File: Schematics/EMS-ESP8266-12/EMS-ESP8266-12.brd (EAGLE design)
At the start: 86 x 50.8 mm, 45 parts, among them IC1 LM393N, J99 Upload, T1 BC547B, T2 BC547B

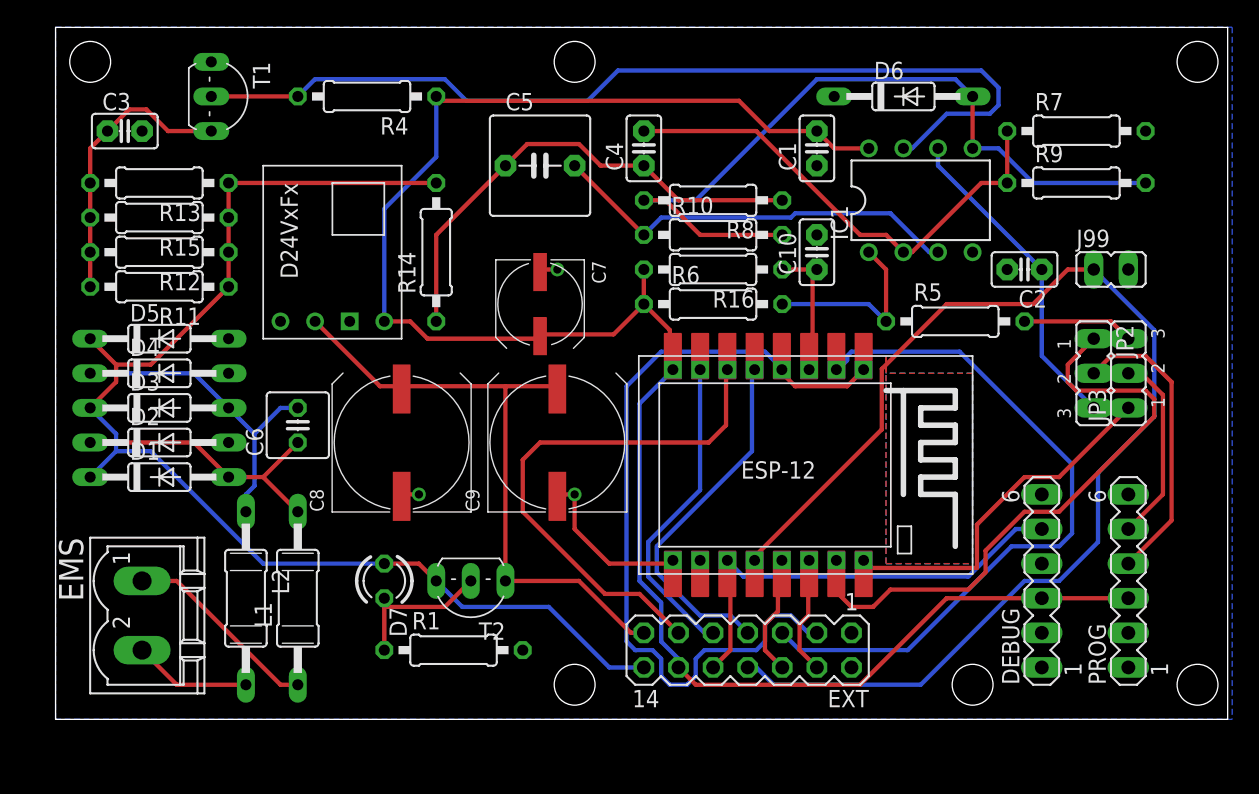
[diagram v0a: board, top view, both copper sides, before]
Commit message: PCB reworked ° remove ground layer below ESP12-antenna ° change connector footprint ° 2pin debug connector ° small form factor for EMS connector
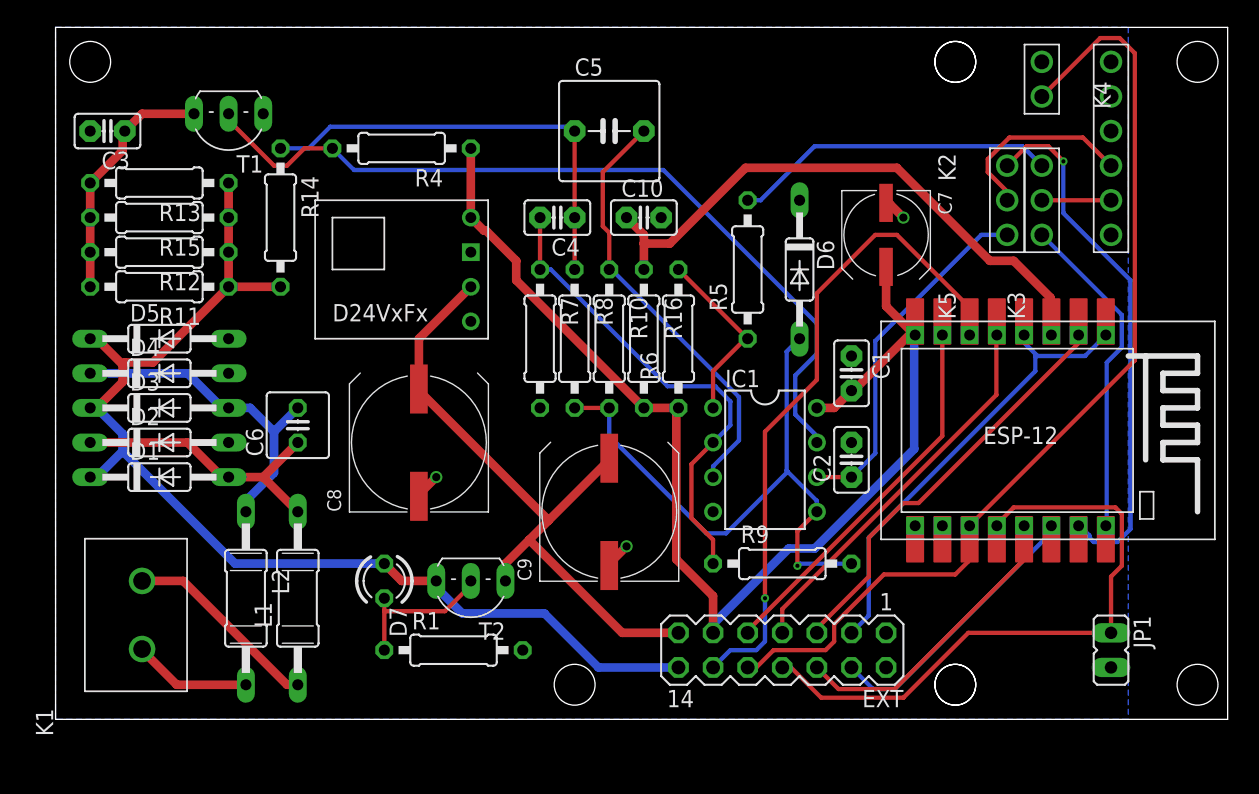
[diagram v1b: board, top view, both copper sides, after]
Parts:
- removed DEBUG: Debug, con-lstb:MA06-1
- removed EMS: (no value), con-phoenix-508:MSTBV2
- removed J99: Upload, jumper:JP1
- removed JP2, JP3: (no value), jumper:JP2
- removed PROG: Program, con-lstb:MA06-1
- added JP1: Upload, jumper:JP1
- added K1: 691102710002, EagleLibrary_Wuerth_Elektronik_eiCan_Terminal_Blocks_Connectors_v6_20150113:691102710002
- added K2: 61300211121, EagleLibrary_Wuerth_Elektronik_eiCan_Board_to_Board_Connectors_v6_20150113:61300211121
- added K3: 61300611121, EagleLibrary_Wuerth_Elektronik_eiCan_Board_to_Board_Connectors_v6_20150113:61300611121
- added K4, K5: 61300311121, EagleLibrary_Wuerth_Elektronik_eiCan_Board_to_Board_Connectors_v6_20150113:61300311121
- moved R7 42.2 mm to (35.6, 27.9), turned to 270 degrees
- moved R9 35.3 mm to (53.3, 11.4)
- moved C7 25.9 mm to (61.0, 35.6)
- moved IC1 22.2 mm to (52.1, 19.1), turned to 270 degrees
- moved C2 18.9 mm to (58.4, 19.1), turned to 90 degrees
- moved U$2 18.0 mm to (85.1, 29.2)
- moved C1 16.7 mm to (58.4, 25.4), turned to 270 degrees
- moved R5 15.7 mm to (50.8, 33.0), turned to 90 degrees
- moved D6 14.8 mm to (54.6, 33.0), turned to 270 degrees
- moved R8 14.4 mm to (38.1, 27.9), turned to 270 degrees
- moved U$1 13.3 mm to (19.1, 27.9), turned to 0 degrees
- moved C10 13.0 mm to (43.2, 36.8), turned to 0 degrees
- moved R14 11.7 mm to (16.5, 36.8), turned to 270 degrees
- moved R10 10.8 mm to (40.6, 27.9), turned to 270 degrees
- moved C4 8.13 mm to (36.8, 36.8), turned to 180 degrees
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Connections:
- net +3V3: now also EXT.11; no longer DEBUG.3, EXT.12, PROG.3
- net EMS_RX: now also K4.3; no longer JP2.3
- net EMS_TX: now also K5.3; no longer JP3.3
- net GND: now also JP1.2, K2.2, K3.6; no longer DEBUG.1, J99.2, PROG.1
- net GPIO0: now also JP1.1; no longer J99.1
- net GPIO12: now also EXT.12; no longer EXT.11
- net GPIO2: now also K2.1; no longer DEBUG.5
- net N$4: now also K1.2; no longer EMS.1
- net N$8: now also K1.1; no longer EMS.2
- net RXD: now also K3.2, K5.2; no longer JP3.2, PROG.5
- net TXD: now also K3.3, K4.2; no longer JP2.2, PROG.4
- net URXD: now also K4.1; no longer JP2.1
- net UTXD: now also K5.1; no longer JP3.1
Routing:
- net +3V3: track 140.8 -> 89.1 mm
- net GPIO0: track 90.8 -> 46.1 mm
- net GPIO2: track 33.5 -> 71.6 mm
- net N$3: track 10.1 -> 43.2 mm
- net REST: track 59.1 -> 33.6 mm
- net ADC: track 51.9 -> 30.5 mm
- net EMS_TX: track 8.15 -> 23.8 mm
- net GPIO5: track 8.92 -> 22.3 mm
- net UREF: track 57.1 -> 45.1 mm, vias 0 -> 1
- net GPIO4: track 8.66 -> 20.6 mm
- net GPIO12: track 39.0 -> 49.0 mm, vias 0 -> 1
- net GND: track 15.3 -> 5.66 mm
- net N$15: track 70.0 -> 60.9 mm
- net RXD: track 14.1 -> 5.08 mm
- net UEMS: track 92.1 -> 84.5 mm
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- removed copper zone on layer 1, net N$10
- removed copper zone on layer 16, net N$10

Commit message: Redesign - Board Rev. 1.0 - Debug Tx Anschluß entfällt, da bereits auf Ext. Port (GPIO2) - CH_PD auf Ext. Port geführt - Längsregler mit LED anstelle 3er Dioden. Als Seiteneffekt gibts eine   Betriebsanzeige - Farbe ganz nach Gusto... - EMS-Tx Ausgang (LM334) auf 100R reduziert - 4x 910R in 2x 470R optimiert - Bestückung kompakter - Boardgröße 77x50 mm² - RC-Kombination CH_PD und REST lt. Espressif HW-SDK
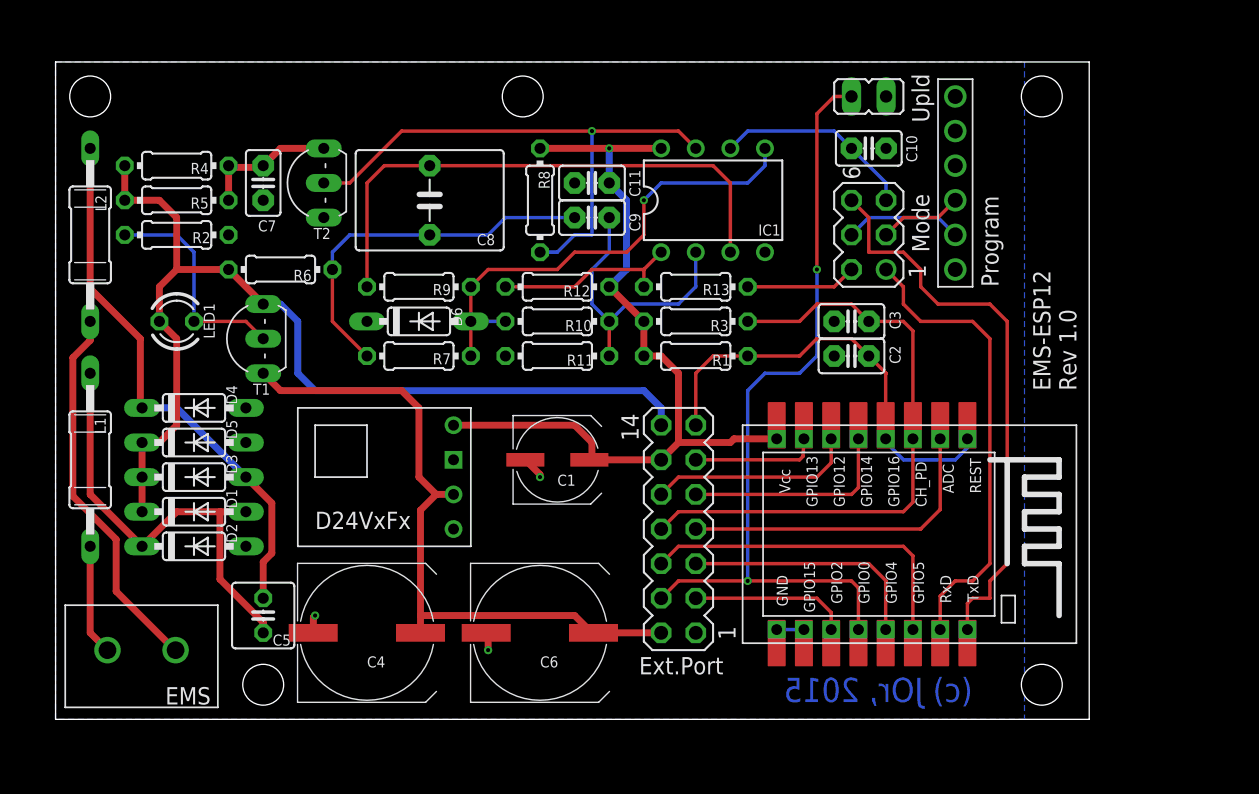
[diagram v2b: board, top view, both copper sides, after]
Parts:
- removed D7: 3mm Rot, led:LED3MM
- removed EXT: (no value), con-lstb:MA07-2
- removed JP1: Upload, jumper:JP1
- removed K1: 691102710002, EagleLibrary_Wuerth_Elektronik_eiCan_Terminal_Blocks_Connectors_v6_20150113:691102710002
- removed K2: 61300211121, EagleLibrary_Wuerth_Elektronik_eiCan_Board_to_Board_Connectors_v6_20150113:61300211121
- removed K3: 61300611121, EagleLibrary_Wuerth_Elektronik_eiCan_Board_to_Board_Connectors_v6_20150113:61300611121
- removed K4, K5: 61300311121, EagleLibrary_Wuerth_Elektronik_eiCan_Board_to_Board_Connectors_v6_20150113:61300311121
- removed R14: 10K, resistor:0207/10
- removed R15: 910R, resistor:0207/10
- removed R16: 3k3, resistor:0207/10
- removed U$1: D24V3F3, buckconv:D24VXFX
- removed U$2: ESP-12ESP-12, ESP8266-ESP12:ESP-12
- added C11: 100n, capacitor-wima:C2.5-2
- added EMS: EMS, EagleLibrary_Wuerth_Elektronik_eiCan_Terminal_Blocks_Connectors_v6_20150113:691102710002
- added ESP1: ESP-12ESP-12, ESP8266-ESP12:ESP-12
- added EXT.PORT: Ext, con-lstb:MA07-2
- added LED1: 3mm, led:LED3MM
- added MOD1: D24V3F3, buckconv:D24VXFX
- added MODE: (no value), con-lstb:MA03-2
- added PROGRAM: 61300611121, EagleLibrary_Wuerth_Elektronik_eiCan_Board_to_Board_Connectors_v6_20150113:61300611121
- added R2: 10K, resistor:0204/7
- added R3: 4k7, resistor:0204/7
- added UPLD: Upload, jumper:JP1
- C1: value 100n -> 220u; device capacitor-wima:C2.5-2 -> rcl:UD-6,3X5,8_NICHICON
- C10: value 100n -> 10n
- C2: value 10n -> 100p
- C3: value 1.5n -> 1n
- C4: value 1n -> 820u; device capacitor-wima:C2.5-2 -> rcl:UD-10X10_NICHICON
- C5: value 10u -> 68p; device capacitor-wima:C5B7.2 -> resistor:C025-050X050
- C6: value 68p -> 820u; device resistor:C025-050X050 -> rcl:UD-10X10_NICHICON
- C7: value 220u -> 1.5n; device rcl:UD-6,3X5,8_NICHICON -> capacitor-wima:C2.5-2
- C8: value 820u -> 10u; device rcl:UD-10X10_NICHICON -> capacitor-wima:C5B11
- C9: value 820u -> 1n; device rcl:UD-10X10_NICHICON -> capacitor-wima:C2.5-2
- D1, D2, D3, D4, D5: value BAT42 -> BAT46; device diode:DO35-10 -> diode:DO35-7
- D6: device diode:DO35-10 -> diode:DO35-7
- R1: value 10K -> 4k7; device resistor:0207/10 -> resistor:0204/7
- R10: value 47K -> 10K; device resistor:0207/10 -> resistor:0204/7
- R11: value 910R -> 100K; device resistor:0207/10 -> resistor:0204/7
- R12: value 910R -> 4K7; device resistor:0207/10 -> resistor:0204/7
- R13: value 910R -> 100; device resistor:0207/10 -> resistor:0204/7
- R4: value 4K7 -> 470R; device resistor:0207/10 -> resistor:0204/7
- R5: value 330 -> 470R; device resistor:0207/10 -> resistor:0204/7
- R6: value 4K7 -> 10K; device resistor:0207/10 -> resistor:0204/7
- R7: value 100K -> 360R; device resistor:0207/10 -> resistor:0204/7
- R8: value 360R -> 4K7; device resistor:0207/10 -> resistor:0204/7
- R9: value 10K -> 47K; device resistor:0207/10 -> resistor:0204/7
- moved C3 56.4 mm to (58.4, 29.2)
- moved C7 45.9 mm to (15.2, 39.4)
- moved C5 43.7 mm to (15.2, 7.62), turned to 90 degrees
- moved R5 42.2 mm to (8.89, 38.1), turned to 0 degrees
- moved R13 40.1 mm to (47.0, 31.8), turned to 0 degrees
- moved C4 33.5 mm to (22.9, 6.35), turned to 0 degrees
- moved R9 33.5 mm to (26.7, 31.8)
- moved T2 32.8 mm to (18.4, 39.4), turned to 90 degrees
- moved R11 29.6 mm to (36.8, 26.7)
- moved R6 29.6 mm to (16.5, 33.0), turned to 180 degrees
- moved R12 29.3 mm to (36.8, 31.8)
- moved L2 29.0 mm to (2.54, 35.6)
- moved D6 28.2 mm to (26.7, 29.2), turned to 0 degrees
- moved R1 28.0 mm to (47.0, 26.7), turned to 180 degrees
- moved C6 23.4 mm to (35.6, 6.35), turned to 0 degrees
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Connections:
- removed net N$3: C10.1, R16.1, U$2.CH_PD
- new net CH_PD: C3.1, ESP1.CH_PD, EXT.PORT.8, R3.1
- new net GPIO15: ESP1.GND, ESP1.GPIO15
- net +3V3: now also C1.+, C11.2, ESP1.VCC, EXT.PORT.12, MOD1.VOUT, R1.2, R12.1, R3.2, R8.1; no longer C1.2, C7.+, EXT.11, R16.2, R4.1, R6.1, U$1.VOUT, U$2.VCC
- net ADC: now also ESP1.ADC, EXT.PORT.7; no longer EXT.5, U$2.ADC
- net EMS_RX: now also C10.1, MODE.5; no longer C2.1, K4.3
- net EMS_TX: now also MODE.2, R13.2; no longer K5.3, R5.2
- net GND: now also C1.-, C11.1, C4.-, C6.-, C7.2, EXT.PORT.1, MOD1.GND, PROGRAM.6, R11.2, R2.2, T2.E, UPLD.1; no longer C1.1, C7.-, C8.-, C9.-, EXT.1, EXT.2, JP1.2, K2.2, K3.6, R1.2, R7.2, T1.E, U$1.GND, U$2.GND, U$2.GPIO15
- net GPIO0: now also ESP1.GPIO0, EXT.PORT.4, UPLD.2; no longer EXT.8, JP1.1, U$2.GPIO0
- net GPIO12: now also ESP1.GPIO12, EXT.PORT.10; no longer EXT.12, U$2.GPIO12
- net GPIO13: now also ESP1.GPIO13, EXT.PORT.11; no longer EXT.9, U$2.GPIO13
- net GPIO14: now also ESP1.GPIO14, EXT.PORT.9; no longer EXT.7, U$2.GPIO14
- net GPIO2: now also ESP1.GPIO2, EXT.PORT.3; no longer EXT.10, K2.1, U$2.GPIO2
- net GPIO4: now also ESP1.GPIO4, EXT.PORT.5; no longer EXT.4, U$2.GPIO4
- net GPIO5: now also ESP1.GPIO5, EXT.PORT.6; no longer EXT.6, U$2.GPIO5
- net N$1: now also C5.1; no longer C6.1
- net N$12: now also C9.2, R10.1, R11.1; no longer C4.2, R7.1, R9.1
- net N$15: now also R8.2, T2.B; no longer R4.2, T1.B
- net N$17: now also LED1.K, R2.1, T1.B; no longer D7.K, R1.1, T2.B
- net N$2: now also C5.2; no longer C6.2
- net N$4: now also EMS.2; no longer K1.2
- net N$5: now also R12.2, R13.1; no longer R5.1, R6.2
- net N$6: now also C7.1, R4.2, R5.2, T2.C; no longer C3.1, R11.2, R12.2, R13.2, R15.2, T1.C
- net N$7: now also C8.1, C9.1, R6.1, R7.1; no longer C4.1, C5.1, R14.1, R8.1
- net N$8: now also EMS.1; no longer K1.1
- net N$9: now also C8.2, R9.1; no longer C5.2, R10.1
- net REST: now also C2.1, ESP1.GPIO16, ESP1.REST, EXT.PORT.13, R1.1; no longer EXT.3, U$2.GPIO16, U$2.REST
- net RXD: now also MODE.4, PROGRAM.2; no longer K3.2, K5.2
- net TXD: now also MODE.3, PROGRAM.3; no longer K3.3, K4.2
- net UBUCK: now also C4.+, C6.+, EXT.PORT.2, MOD1.VIN, T1.E; no longer C8.+, C9.+, EXT.13, T2.E, U$1.VIN
- net UEMS: now also EXT.PORT.14, LED1.A, R4.1, R5.1, R6.2, T1.C; no longer D7.A, EXT.14, R11.1, R12.1, R13.1, R14.2, R15.1, T2.C
- net UREF: now also R7.2; no longer R8.2
- net URXD: now also ESP1.RXD, MODE.1; no longer K4.1, U$2.RXD
- net UTXD: now also ESP1.TXD, MODE.6; no longer K5.1, U$2.TXD
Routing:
- net GPIO2: track 71.6 -> 11.6 mm
- net CH_PD: track 0.00 -> 45.3 mm
- net N$3: track 43.2 -> 0.00 mm
- net GPIO12: track 49.0 -> 15.2 mm, vias 1 -> 0
- net +3V3: track 89.1 -> 60.8 mm, vias 0 -> 1
- net N$15: track 60.9 -> 41.4 mm, vias 0 -> 1
- net N$8: track 8.75 -> 27.8 mm
- net GPIO13: track 27.8 -> 9.27 mm
- net UTXD: track 24.3 -> 41.9 mm
- net N$2: track 24.5 -> 40.3 mm
- net EMS_TX: track 23.8 -> 8.15 mm
- net N$12: track 35.5 -> 21.2 mm
- net GPIO0: track 46.1 -> 59.2 mm, vias 0 -> 2
- net GPIO14: track 28.4 -> 15.7 mm
- net N$1: track 20.9 -> 33.2 mm
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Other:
- board size 86 x 50.8 mm -> 75.9 x 48.2 mm
- board text added: "(c) JOr, 2015"
- board text added: "EMS-ESP12 Rev 1.0"
- board text added: "Ext.Port"
- board text added: "Mode"
- board text added: "Program"
- board text added: "Upld"
